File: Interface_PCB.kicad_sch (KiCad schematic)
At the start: 44 parts, among them IC1 STM32L412RBT6P, J1 Conn_01x04, J2 Conn_01x04, J3 Conn_01x04, J4 Conn_01x04, J5 AVR-JTAG-10, J6 Micro_SD_Card, J7 USB_B, U1 AMS1117-3.3, Y1 Crystal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

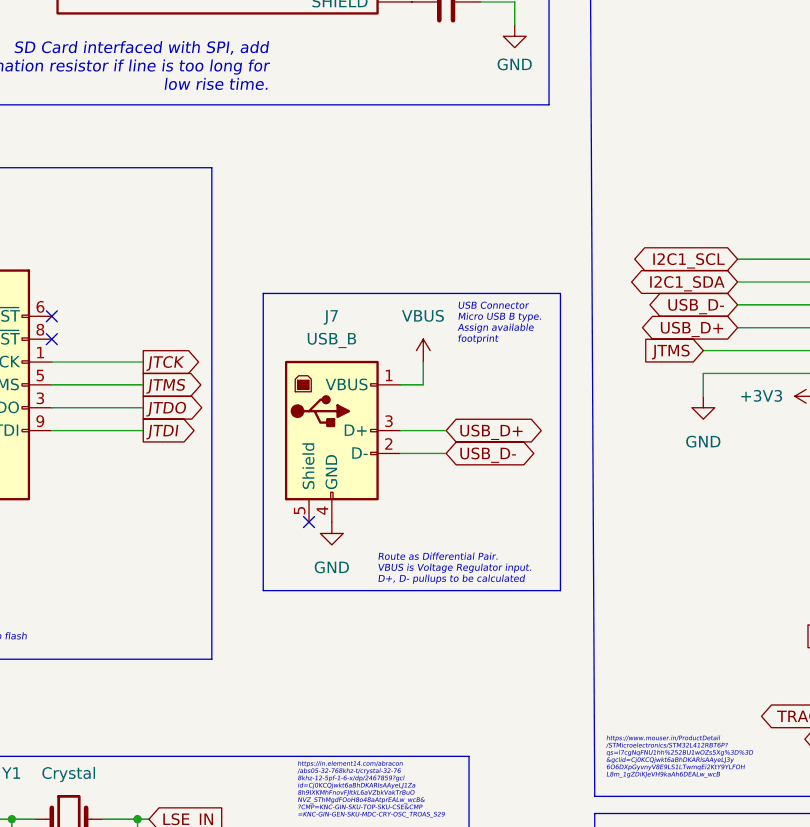
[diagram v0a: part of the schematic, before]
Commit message: Resistor pads to SD card connector
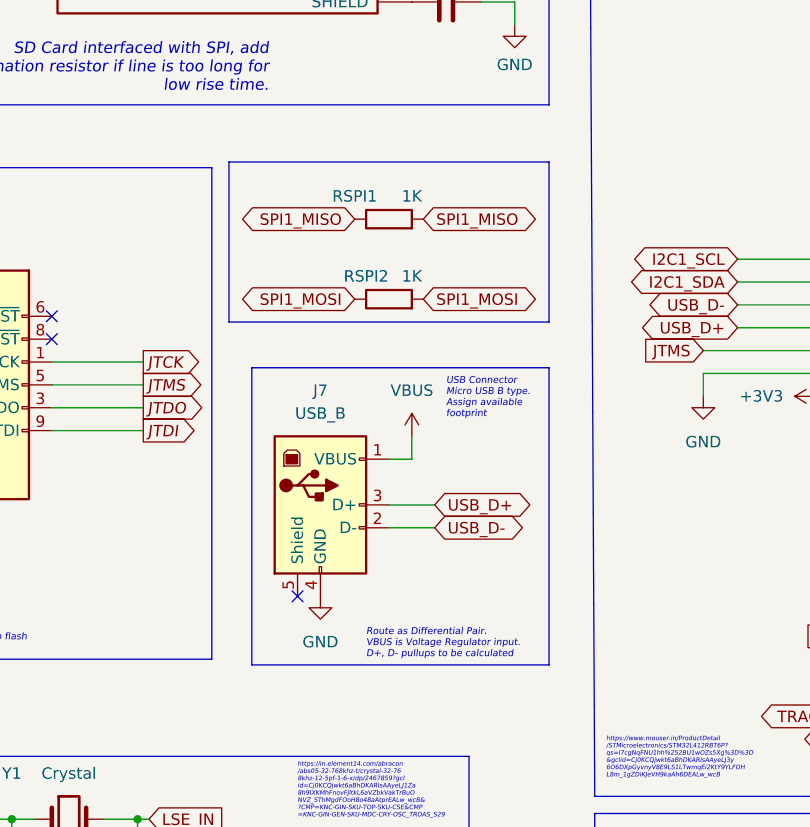
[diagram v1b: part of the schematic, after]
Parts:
- added RSPI1, RSPI2: 1K, Resistor_SMD:R_0402_1005Metric, symbol Device:R
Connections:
- net SPI1_MISO: now also RSPI1.1, RSPI1.2
- net SPI1_MOSI: now also RSPI2.1, RSPI2.2
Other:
- moved on the sheet: J7

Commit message: Added BOM, position and gerber files
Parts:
- LMS1: footprint Capacitor_SMD:C_0603_1608Metric -> Inductor_SMD:L_0603_1608Metric
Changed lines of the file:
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@@
     (property "Reference" "LMS1" (id 0) (at 42.545 168.91 90))
     (property "Value" "39nH" (id 1) (at 42.545 171.45 90))
-    (property "Footprint" "Capacitor_SMD:C_0603_1608Metric" (id 2) (at 42.545 173.99 0)
+    (property "Footprint" "Inductor_SMD:L_0603_1608Metric" (id 2) (at 42.545 173.99 0)
       (effects (font (size 1.27 1.27)) hide)
     )
@@
   )
   (symbol (lib_id "Device:L") (at 35.56 95.25 90) (unit 1)
-    (in_bom yes) (on_board yes) (fields_autoplaced)
+    (in_bom yes) (on_board yes)
     (property "Reference" "LR1" (id 0) (at 35.56 91.44 90))
-    (property "Value" "39nH" (id 1) (at 35.56 91.44 90)
-      (effects (font (size 1.27 1.27)) hide)
-    )
+    (property "Value" "39nH" (id 1) (at 35.56 96.52 90))
     (property "Footprint" "Inductor_SMD:L_0402_1005Metric" (id 2) (at 35.56 95.25 0)
       (effects (font (size 1.27 1.27)) hide)
@@
     )
     (path "/18637ffa-547f-4cbc-abb9-10778450da01"
-      (reference "LMS1") (unit 1) (value "39nH") (footprint "Capacitor_SMD:C_0603_1608Metric")
+      (reference "LMS1") (unit 1) (value "39nH") (footprint "Inductor_SMD:L_0603_1608Metric")
     )
     (path "/8ece260d-199e-44fd-956a-d40950c3f424"
